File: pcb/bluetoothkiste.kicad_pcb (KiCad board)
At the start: 2 copper layers, 44.9 x 95.6 mm, 62 parts, among them J1 DB9_Female, J2 Screw_Terminal_01x03, J3 Conn_01x04_Female, J4 RJ45, J5 USB_A, J6 Conn_01x04_Female, J7 Conn_01x03, J8 Conn_01x03, U1 L7805, U2 MAX232

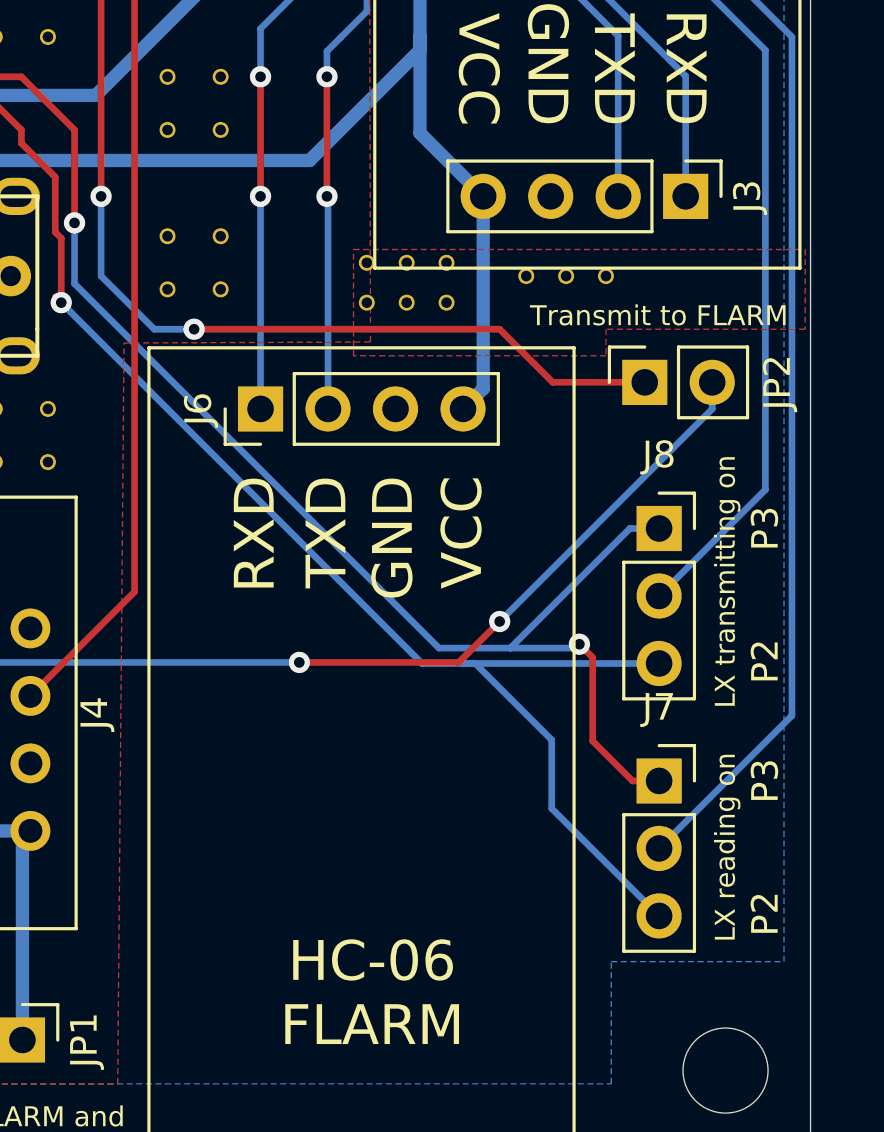
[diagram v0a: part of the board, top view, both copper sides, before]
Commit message: footprints updated
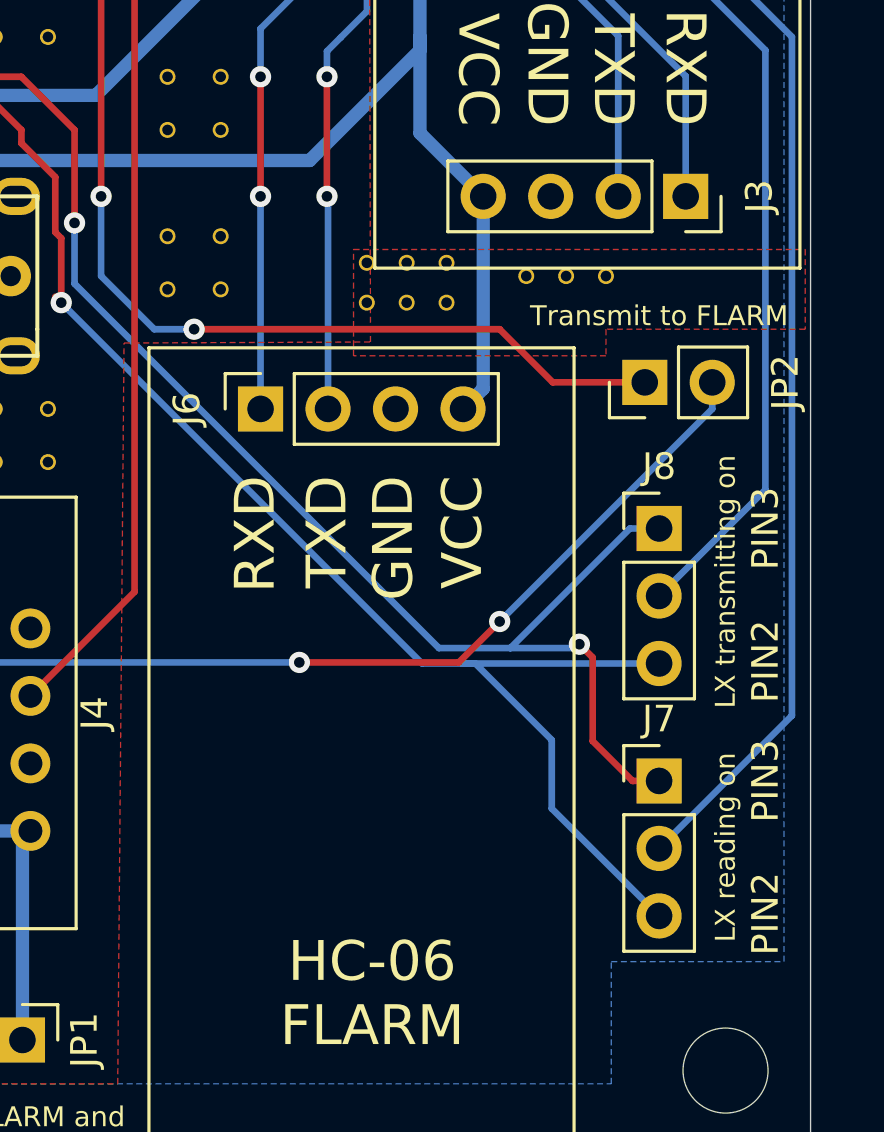
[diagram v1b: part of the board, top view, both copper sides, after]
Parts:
- J3, J6: footprint Connector_PinHeader_2.54mm:PinHeader_1x04_P2.54mm_Vertical -> Connector_PinSocket_2.54mm:PinSocket_1x04_P2.54mm_Vertical
- J7, J8: footprint Connector_PinSocket_2.54mm:PinSocket_1x03_P2.54mm_Vertical -> Connector_PinHeader_2.54mm:PinHeader_1x03_P2.54mm_Vertical
- JP2: footprint Connector_PinSocket_2.54mm:PinSocket_1x02_P2.54mm_Vertical -> Connector_PinHeader_2.54mm:PinHeader_1x02_P2.54mm_Vertical
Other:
- board text added: "PIN2"
- board text added: "PIN3"
- board text removed: "P2"
- board text removed: "P3"

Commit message: kicad 9
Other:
- net class Broader removed
- net class Default removed
